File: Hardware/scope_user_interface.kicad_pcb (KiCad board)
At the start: 2 copper layers, 275 x 100 mm, 111 parts, among them J1 USB_B_Micro, SW1 SW_Push, SW10 SW_Push, SW11 SW_Push, SW12 SW_Push, SW13 SW_Push, SW14 SW_Push, SW18 Rotary_Encoder_Switch, SW19 Rotary_Encoder_Switch, SW2 SW_Push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

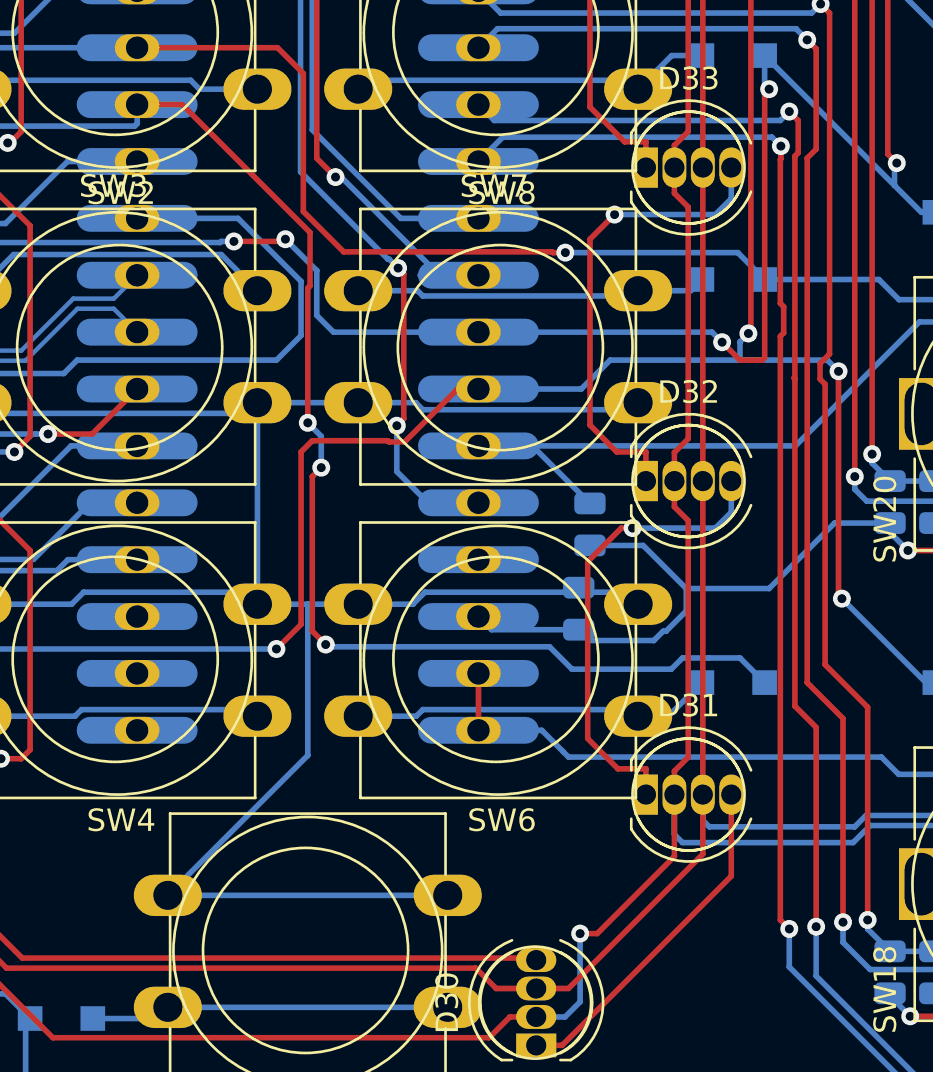
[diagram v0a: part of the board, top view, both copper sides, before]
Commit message: Changed encoder3b to PB12
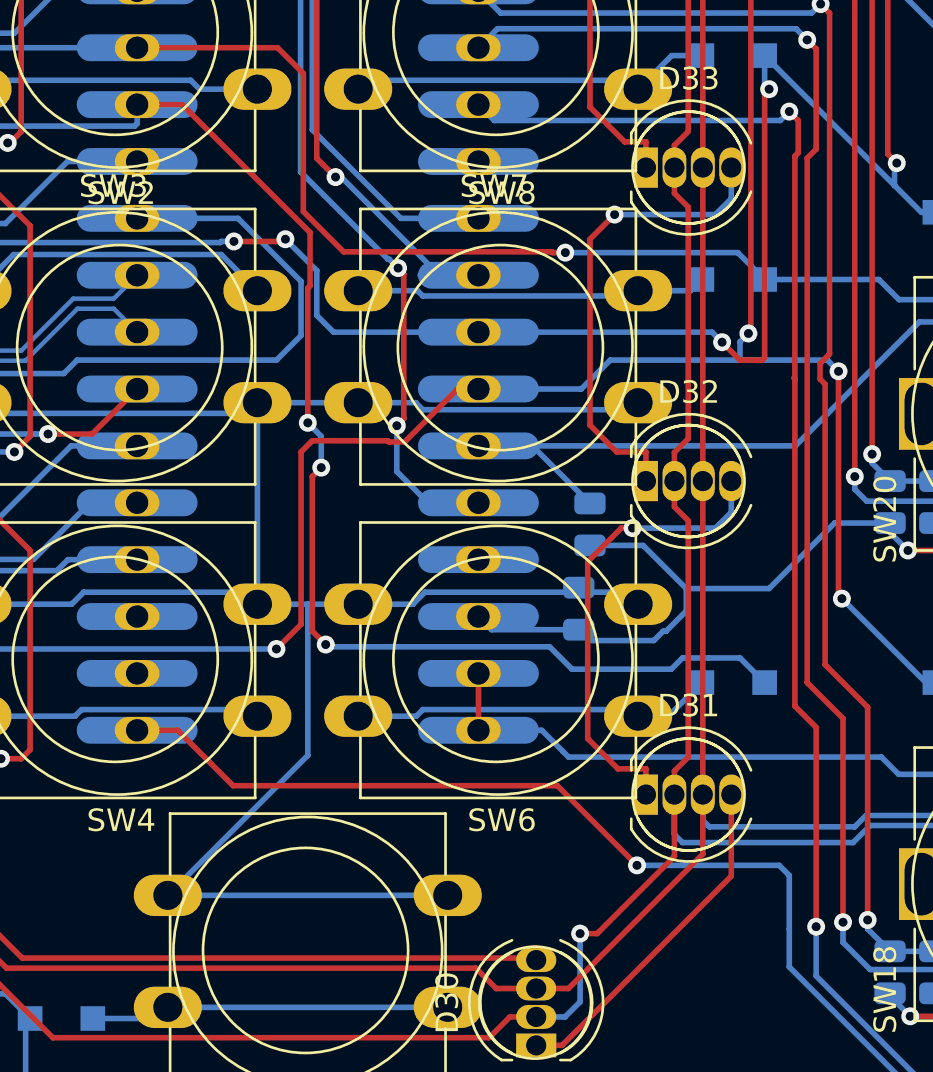
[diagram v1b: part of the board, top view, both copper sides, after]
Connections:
- U1 pad 1: Net-(U1-Pad1) -> /encoder3b
- U1 pad 30: /encoder3b -> Net-(U1-Pad30)
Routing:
- net /encoder3b: track 95.7 -> 80.5 mm, vias 2 -> 1
